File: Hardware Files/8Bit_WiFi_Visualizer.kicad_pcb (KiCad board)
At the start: 2 copper layers, 59 x 44.5 mm, 34 parts, among them J1 USB_B_Micro, J2 Conn_01x04, SW1 SW_Push_Dual, SW2 SW_SPST, SW3 SW_SPST, U1 3.3V 1A, U2 74HC595, U3 ESP-WROOM-02D

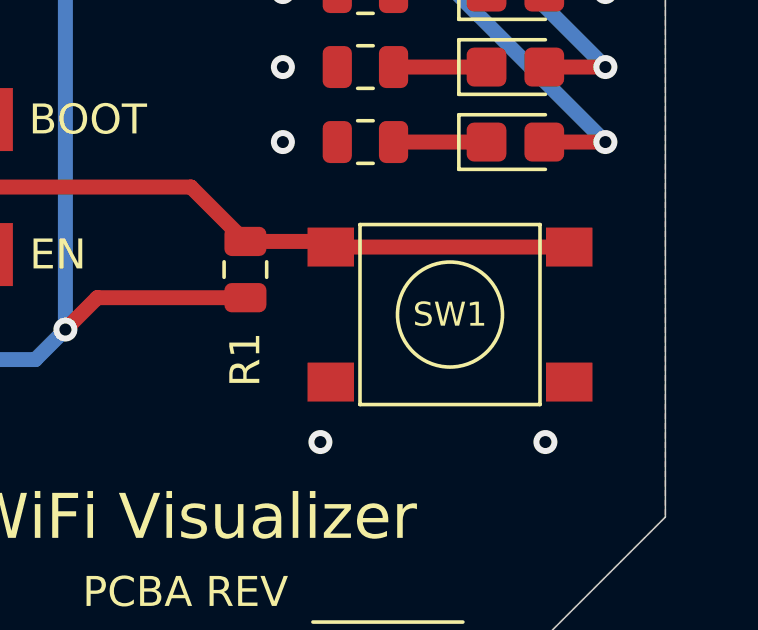
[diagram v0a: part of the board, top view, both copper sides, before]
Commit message: Update tactile switch footprint to include 3D model
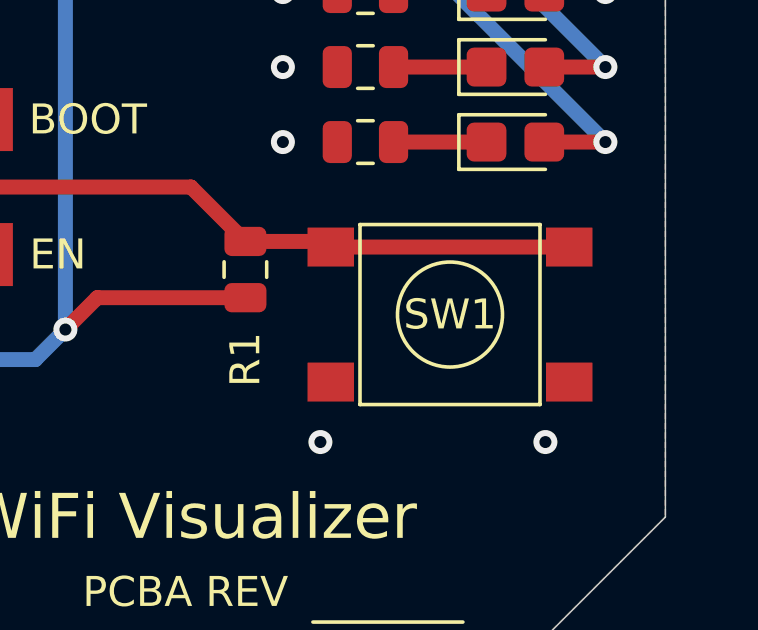
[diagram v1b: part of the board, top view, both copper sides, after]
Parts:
- SW1: footprint 8Bit_WiFi_Visualizer_Footprints:PTS645SK50SMTR92 LFS -> 8Bit_WiFi_Visualizer_Footprints:PTS645SK50SMTR92LFS

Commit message: Change to 1206 components and reroute
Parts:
- removed R2, R3, R4, R5, R6, R7, R8, R9: 75R, Resistor_SMD:R_0805_2012Metric
- added J3: Conn_01x01, MountingHole:MountingHole_3.2mm_M3_DIN965_Pad, F.Cu at (5.00, 5.00)
- added J4: Conn_01x01, MountingHole:MountingHole_3.2mm_M3_DIN965_Pad, F.Cu at (55.0, 5.00)
- C2, C3, C4, C5, C6: footprint Capacitor_SMD:C_0805_2012Metric -> Capacitor_SMD:C_1206_3216Metric_Pad1.42x1.75mm_HandSolder
- D1, D2, D3, D4, D5, D6, D7, D8: footprint LED_SMD:LED_0805_2012Metric_Castellated -> LED_SMD:LED_1206_3216Metric_Pad1.42x1.75mm_HandSolder
- R1, R10, R11, R12, R13: footprint Resistor_SMD:R_0805_2012Metric -> Resistor_SMD:R_1206_3216Metric_Pad1.42x1.75mm_HandSolder
- moved R1 217.5 mm to (23.5, 29.0), turned to 270 degrees
- moved U1 202.0 mm to (12.8, 24.8), turned to 0 degrees
- moved SW2 200.8 mm to (21.0, 38.0), turned to 180 degrees
- moved SW3 200.7 mm to (21.0, 34.0), turned to 180 degrees
- moved D8 197.7 mm to (52.2, 11.2)
- moved D7 197.5 mm to (52.2, 14.2)
- moved C3 197.4 mm to (9.50, 31.8), turned to 270 degrees
- moved D6 197.3 mm to (52.2, 17.2)
- moved D5 197.1 mm to (52.2, 20.2)
- moved D4 197.0 mm to (52.2, 23.2)
- moved D3 196.8 mm to (52.2, 26.2)
- moved SW1 196.7 mm to (49.8, 38.0)
- moved D2 196.6 mm to (52.2, 29.2)
- moved D1 196.4 mm to (52.2, 32.2)
- moved J1 195.3 mm to (2.70, 15.0)
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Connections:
- D1 pad 1: Net-(D1-Pad1) -> GND
- D2 pad 1: Net-(D2-Pad1) -> GND
- D3 pad 1: Net-(D3-Pad1) -> GND
- D4 pad 1: Net-(D4-Pad1) -> GND
- D5 pad 1: Net-(D5-Pad1) -> GND
- D6 pad 1: Net-(D6-Pad1) -> GND
- D7 pad 1: Net-(D7-Pad1) -> GND
- D8 pad 1: Net-(D8-Pad1) -> GND
- U3 pad 10: /DATA -> /CLOCK
- U3 pad 17: Net-(U3-Pad17) -> /DATA
- U3 pad 7: /CLOCK -> Net-(U3-Pad7)
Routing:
- net +3V3: track 97.1 -> 56.8 mm, vias 23 -> 21
- net /LATCH: track 5.17 -> 26.2 mm, vias 0 -> 2
- net /ESP_TX: track 36.1 -> 56.1 mm, vias 0 -> 1
- net /DATA: track 8.69 -> 28.6 mm, vias 0 -> 2
- net /ESP_RX: track 36.7 -> 55.4 mm, vias 0 -> 1
- net /ESP_EN: track 37.2 -> 55.1 mm
- net /CLOCK: track 26.0 -> 13.5 mm
- net GND: track 9.27 -> 0.00 mm, vias 15 -> 7
- net /CLEAR: track 22.6 -> 31.4 mm
- net /LED_8: track 15.6 -> 22.1 mm
- net /BOOT: track 26.5 -> 20.2 mm
- net /LED_7: track 15.3 -> 20.5 mm
- net +5V: track 34.2 -> 29.0 mm, vias 2 -> 0
- net /SW_1: track 53.4 -> 57.5 mm, vias 2 -> 3
- net /LED_6: track 15.8 -> 19.3 mm
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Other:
- board size 59 x 44.5 mm -> 60 x 45 mm
- board text added: "STASIS"

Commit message: Update Logo
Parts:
- added G***: LOGO, 8Bit_WiFi_Visualizer_Footprints:logo, F.Cu at (35.0, 38.0)
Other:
- board text removed: "STASIS"
